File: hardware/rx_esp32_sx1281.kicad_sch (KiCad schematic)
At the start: 24 parts, among them SW1 SKUBAAE010, U16 ESP32-PICO-V3, U18 SX1281, X3 52MHz TCXO

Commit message: Preserve owner schematic and board before final design review
Snapshot of the saved working design supplied for review.
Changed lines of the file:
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@@
-	)
-	(junction
-		(at 54.61 119.38)
-		(diameter 0)
-		(color 0 0 0 0)
 	)
 	(junction
@@
 	)
 	(junction
-		(at 96.52 59.69)
-		(diameter 0)
-		(color 0 0 0 0)
-	)
-	(junction
 		(at 246.38 167.64)
 		(diameter 0)
 		(color 0 0 0 0)
-	)
-	(junction
-		(at 96.52 52.07)
-		(diameter 0)
-		(color 0 0 0 0)

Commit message: Correct Whoop schematic and prepare component library for routing
Add local BMI270 bypassing, improve regulator capacitance margin, isolate
bidirectional DShot supply domains, and correct PA reference accuracy.
Remove Q28/R11 with matching firmware polarity and retain the proven
OpenFC-Lite OSD topology. Correct the receiver LED bypass rail.

Synchronize PCB connectivity, verify component pins and land patterns,
and provide firmware bindings plus placement/layer guidance. Replace stale
manual BOM and interface plans with schematic-derived exports.

Validation: ERC 0, seven netlist checks, 48 footprint checks, 22 rule
behavior cases, and PCB schematic parity 0. The parked PCB retains layout
DRC findings and 499 unconnected items; no manufacturing or flight release.
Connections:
- net +3.3V: no longer C83.1
- net +5V: now also C83.1
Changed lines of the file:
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@@
 		)
 	)
-	(text_box "D4 RGB LED (GPIO32) on +3.3V, 0.2 V under the datasheet VDD minimum: bench-check; fallback VDD to +5V."
+	(text_box "D4 RGB LED (GPIO32): +5V supply, C83 100nF local bypass. Specified DIN VIH = 2.8V; direct 3.3V data is valid. Place C83 beside D4 VDD/GND."
 		(exclude_from_sim no)
 		(at 38.1 215.9 0)
@@
 			)
 		)
-		(property "Description" "ESP32-PICO-V3 SiP: ESP32 (chip rev v3) + 4 MB in-package SPI flash + 40 MHz crystal + RF match and bypass capacitors, Wi-Fi + Bluetooth, LGA-48 7 x 7 mm, 0.5 mm pitch, EP 49 = GND; -40..85 C ambient (in-package flash). In-package flash \n\n(datasheet v1.3 Table 5, Fig 8): CMD/IO11 (30) and CLK/IO6 (31) are wired to it, leave them unconnected (no-connect flag, Fig 11 note); GPIO16/17/18/23 drive it inside the SiP and are not exposed. NC pins 25, 35, 36, 44, 45, 47, 48 (Table 4). VDD_SDIO (26) powers the flash internally: leave unconnected (Fig 11). MTDI/IO12 must read 0 at reset (3.3 V flash, Fig 11 note). I34-I39 input only. Alternate ESP32-PICO-V3-02 (same pinout; pins 28/29 then drive in-package PSRAM)"
+		(property "Description" "ESP32-PICO-V3 SiP: ESP32 (chip rev v3) + 4 MB in-package SPI flash + 40 MHz crystal + RF match and bypass capacitors, Wi-Fi + Bluetooth, LGA-48 7 x 7 mm, 0.5 mm pitch, EP 49 = GND; -40..85 C ambient (in-package flash). In-package flash \n\n\n\n(datasheet v1.3 Table 5, Fig 8): CMD/IO11 (30) and CLK/IO6 (31) are wired to it, leave them unconnected (no-connect flag, Fig 11 note); GPIO16/17/18/23 drive it inside the SiP and are not exposed. NC pins 25, 35, 36, 44, 45, 47, 48 (Table 4). VDD_SDIO (26) powers the flash internally: leave unconnected (Fig 11). MTDI/IO12 must read 0 at reset (3.3 V flash, Fig 11 note). I34-I39 input only. Alternate ESP32-PICO-V3-02 (same pinout; pins 28/29 then drive in-package PSRAM)"
 			(at 243.84 215.9 0)
 			(hide yes)
@@
 	)
 	(symbol
-		(lib_id "power:+3.3V")
+		(lib_id "power:+5V")
 		(at 71.12 196.85 0)
 		(unit 1)
@@
 			)
 		)
-		(property "Value" "+3.3V"
+		(property "Value" "+5V"
 			(at 71.12 193.294 0)
 			(show_name no)

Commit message: Preserve owner schematic and placement edits before GPIO remap
Retain the saved layout, OSD bypass addition and component removals exactly
as received. This snapshot separates owner changes from the GPIO remap.
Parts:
- removed C132, C133: 1.2pF, lib:C_0201_0603Metric_L, symbol Device:C
- removed R88: 0R, lib:R_0201_0603Metric_L, symbol Device:R
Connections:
- net RF_WIFI_ANT is gone; now on net RF_WIFI: AE2.1 (FEED), AE2.4 (FEED)

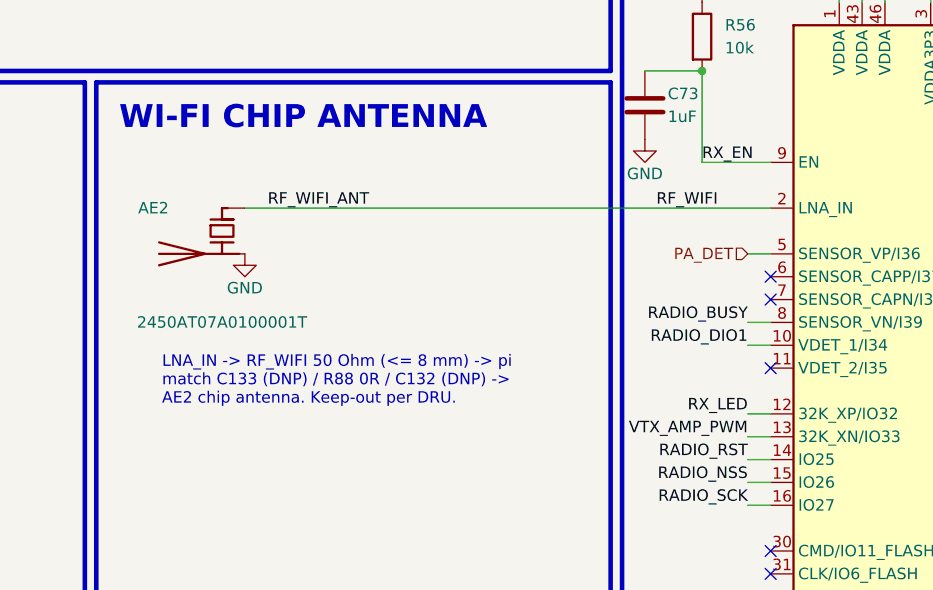
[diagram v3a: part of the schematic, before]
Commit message: Route local ESC and VTX connections and compact Wi-Fi antenna layout
Add the fitted series link and two optional matching lands. Replace the large antenna reservation with a documented compact prototype window and shorten its feed. Preserve motor connector and half-bridge placement.

Integrate checked ESC gate/BEMF, boost and VTX copper, with filled and capped staggered HDI vias and local ground references. Remove stale layout guidance and refresh schematic exports.

137 connection groups pass. Native DRC has no copper errors or schematic parity findings; 138 existing warnings and 468 open connections remain. Routing and RF performance validation are incomplete.
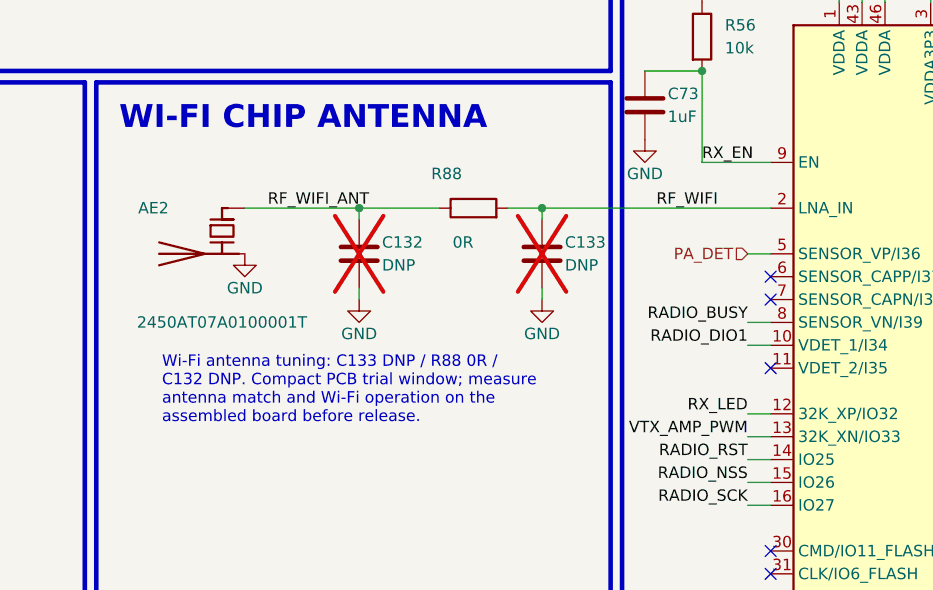
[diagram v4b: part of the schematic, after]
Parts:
- added C132, C133: DNP, lib:C_0201_0603Metric_L, symbol Device:C
- added R88: 0R, lib:R_0201_0603Metric_L, symbol Device:R
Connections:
- net GND: now also C132.2, C133.2
- net RF_WIFI: now also C133.1, R88.2; no longer AE2.1 (FEED), AE2.4 (FEED)
- new net RF_WIFI_ANT: AE2.1 (FEED), AE2.4 (FEED), C132.1, R88.1

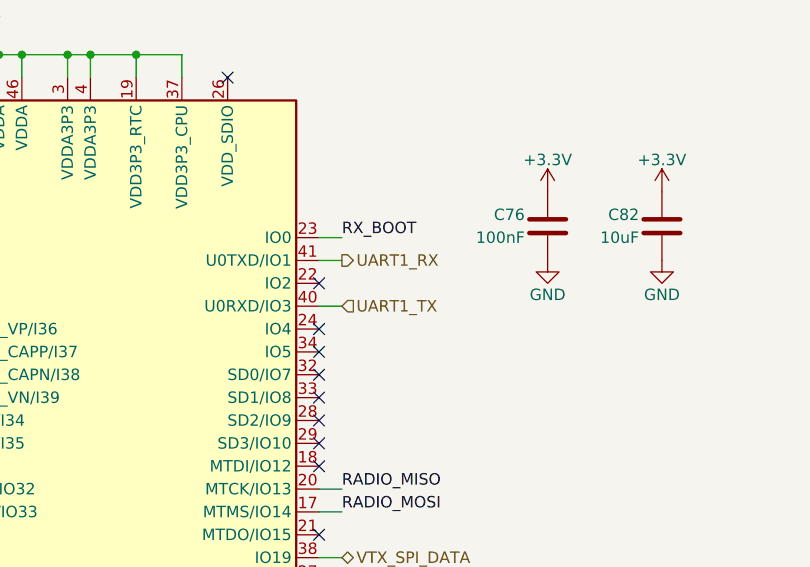
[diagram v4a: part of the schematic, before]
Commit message: Place receiver on south UART and HD on east UART
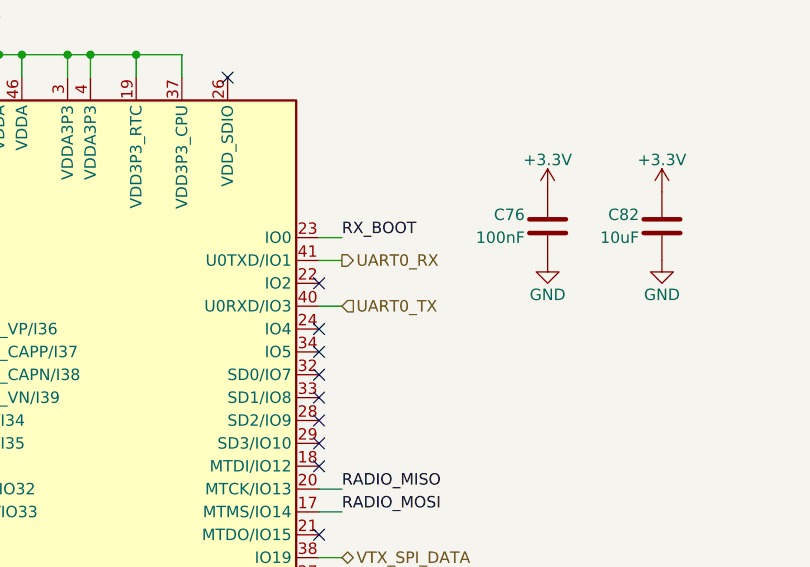
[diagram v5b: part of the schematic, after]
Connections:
- net UART1_RX renamed UART0_RX
- net UART1_TX renamed UART0_TX
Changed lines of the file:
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@@
 		)
 	)
-	(hierarchical_label "UART1_TX"
+	(hierarchical_label "UART0_TX"
 		(shape input)
 		(at 269.24 195.58 0)
@@
 		)
 	)
-	(hierarchical_label "UART1_RX"
+	(hierarchical_label "UART0_RX"
 		(shape output)
 		(at 269.24 190.5 0)
